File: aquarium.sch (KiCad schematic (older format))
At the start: 39 parts, among them U1 MOC3063, U2 MOC3063

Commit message: ATmega48PA changet to ATmega8A
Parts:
- DD4: value ATMEGA48PA -> ATMEGA8A; symbol ATMEGA48PA_EXT -> ATMEGA8_EXT
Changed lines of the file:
@@
 $EndDescr
 $Comp
-L ATMEGA48PA_EXT DD4
+L ATMEGA8_EXT DD4
 U 1 1 5677FF09
 P 10150 2900
 F 0 "DD4" H 10150 5101 138 0000 C CNN
-F 1 "ATMEGA48PA" H 10150 4886 138 0000 C CNN
+F 1 "ATMEGA8A" H 10150 4886 138 0000 C CNN
 F 2 "Микросхемы:TQFP32-30" H 10150 4831 60  0001 C CNN
 F 3 "" H 10150 3150 60  0001 C CNN

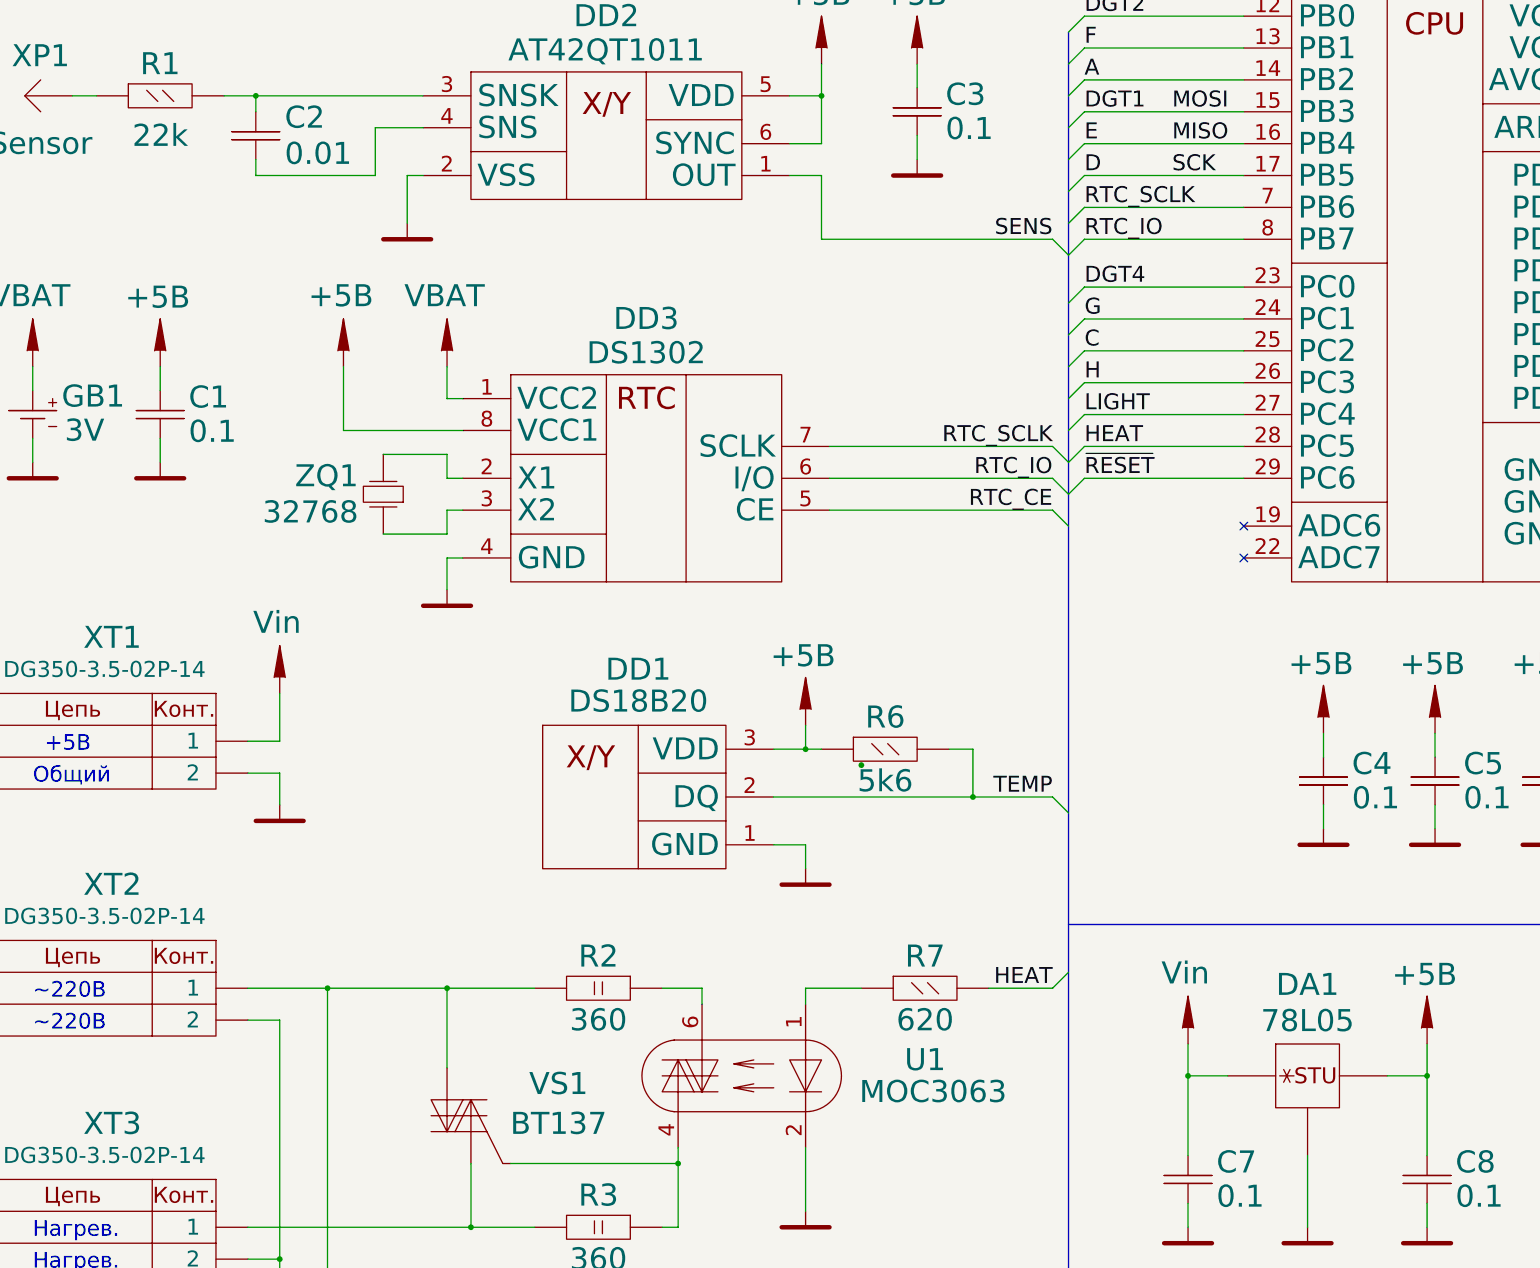
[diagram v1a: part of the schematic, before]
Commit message: Corrected sensitivity of the sensor and added noise protection on Reset pin.
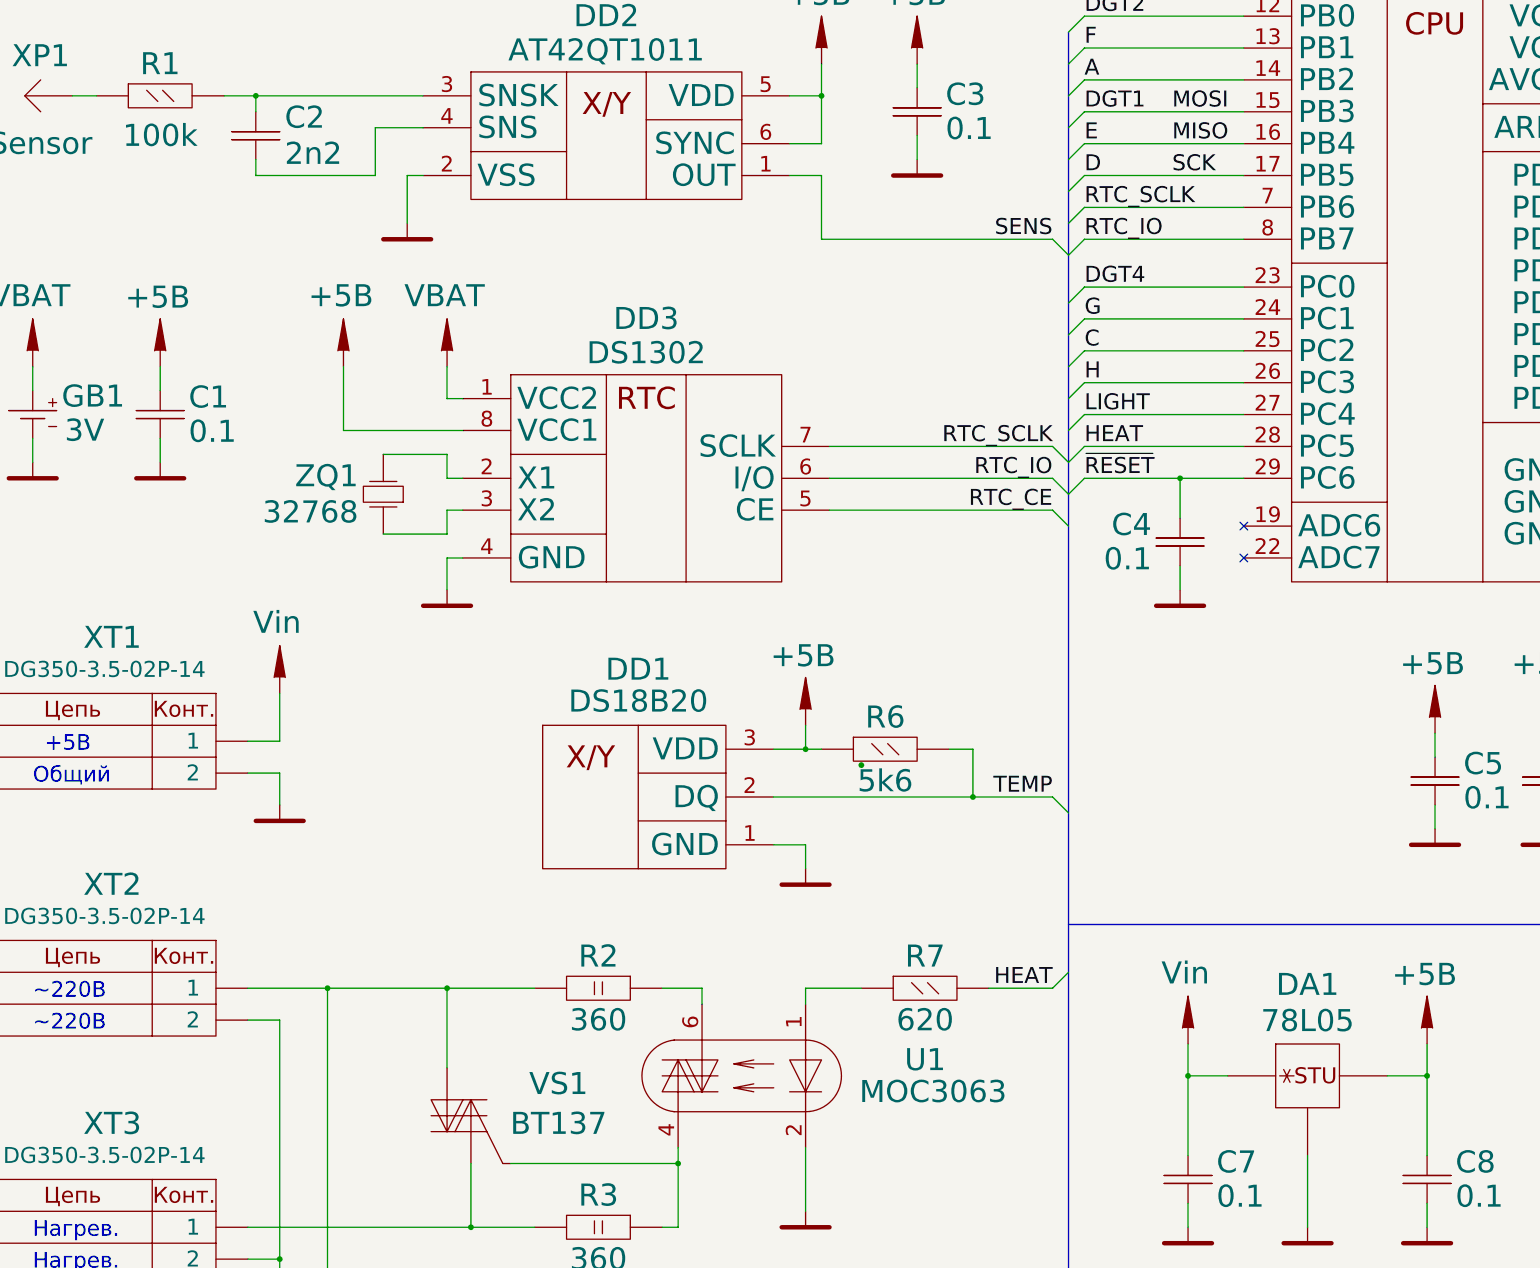
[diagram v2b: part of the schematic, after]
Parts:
- C2: value 0.01 -> 2n2
- R1: value 22k -> 100k
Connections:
- net +5B: no longer C4.1
- net ~RESET: now also C4.1
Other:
- moved on the sheet: C4
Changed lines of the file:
@@
 L C C4
 U 1 1 5679197E
-P 9450 6000
-F 0 "C4" H 9628 6108 138 0000 L CNN
-F 1 "0.1" H 9628 5893 138 0000 L CNN
-F 2 "Конденсаторы:SMD_0805" H 9450 6025 60  0001 C CNN
-F 3 "" H 9450 6025 60  0000 C CNN
-	1    9450 6000
-	1    0    0    -1
+P 8550 4500
+F 0 "C4" H 8728 4608 138 0000 L CNN
+F 1 "0.1" H 8728 4393 138 0000 L CNN
+F 2 "Конденсаторы:SMD_0805" H 8550 4525 60  0001 C CNN
+F 3 "" H 8550 4525 60  0000 C CNN
+	1    8550 4500
+	-1   0    0    -1
 $EndComp
 $Comp
@@
 L GND #PWR01
 U 1 1 56791BC2
-P 9450 6300
-F 0 "#PWR01" H 9850 6300 138 0001 C CNN
-F 1 "GND" H 9100 6300 138 0001 C CNN
-F 2 "" H 9450 6300 60  0000 C CNN
-F 3 "" H 9450 6300 60  0000 C CNN
-	1    9450 6300
-	1    0    0    -1
+P 8550 4800
+F 0 "#PWR01" H 8950 4800 138 0001 C CNN
+F 1 "GND" H 8200 4800 138 0001 C CNN
+F 2 "" H 8550 4800 60  0000 C CNN
+F 3 "" H 8550 4800 60  0000 C CNN
+	1    8550 4800
+	-1   0    0    -1
 $EndComp
 $Comp
@@
 $Comp
 L +5B #PWR04
-U 1 1 56791C22
-P 9450 5700
-F 0 "#PWR04" H 9950 5800 138 0001 C CNN
-F 1 "+5B" H 9434 6135 138 0000 C CNN
-F 2 "" H 9450 5900 60  0000 C CNN
-F 3 "" H 9450 5900 60  0000 C CNN
-	1    9450 5700
-	1    0    0    -1
-$EndComp
-$Comp
-L +5B #PWR05
 U 1 1 56791C40
 P 10150 5700
-F 0 "#PWR05" H 10650 5800 138 0001 C CNN
+F 0 "#PWR04" H 10650 5800 138 0001 C CNN
 F 1 "+5B" H 10134 6135 138 0000 C CNN
 F 2 "" H 10150 5900 60  0000 C CNN
@@
 $EndComp
 $Comp
-L +5B #PWR06
+L +5B #PWR05
 U 1 1 56791C61
 P 10850 5700
-F 0 "#PWR06" H 11350 5800 138 0001 C CNN
+F 0 "#PWR05" H 11350 5800 138 0001 C CNN
 F 1 "+5B" H 10834 6135 138 0000 C CNN
 F 2 "" H 10850 5900 60  0000 C CNN
@@
 $EndComp
 Wire Wire Line
-	9450 5700 9450 5850
-Wire Wire Line
-	9450 6150 9450 6300
+	8550 4100 8550 4350
+Wire Wire Line
+	8550 4650 8550 4800
 Wire Wire Line
 	10150 5700 10150 5850
@@
 	10850 6150 10850 6300
 $Comp
-L +5B #PWR07
+L +5B #PWR06
 U 1 1 56791F4C
 P 11550 1000
-F 0 "#PWR07" H 12050 1100 138 0001 C CNN
+F 0 "#PWR06" H 12050 1100 138 0001 C CNN
 F 1 "+5B" H 11534 1435 138 0000 C CNN
 F 2 "" H 11550 1200 60  0000 C CNN
@@
 Connection ~ 11550 1200
 $Comp
-L GND #PWR08
+L GND #PWR07
 U 1 1 567920EA
 P 11550 4800
-F 0 "#PWR08" H 11950 4800 138 0001 C CNN
+F 0 "#PWR07" H 11950 4800 138 0001 C CNN
 F 1 "GND" H 11200 4800 138 0001 C CNN
 F 2 "" H 11550 4800 60  0000 C CNN
@@
 $EndComp
 $Comp
-L GND #PWR09
+L GND #PWR08
 U 1 1 56795326
 P 6900 2100
-F 0 "#PWR09" H 7300 2100 138 0001 C CNN
+F 0 "#PWR08" H 7300 2100 138 0001 C CNN
 F 1 "GND" H 6550 2100 138 0001 C CNN
 F 2 "" H 6900 2100 60  0000 C CNN
@@
 $EndComp
 $Comp
-L +5B #PWR010
+L +5B #PWR09
 U 1 1 5679532C
 P 6900 1500
-F 0 "#PWR010" H 7400 1600 138 0001 C CNN
+F 0 "#PWR09" H 7400 1600 138 0001 C CNN
 F 1 "+5B" H 6884 1935 138 0000 C CNN
 F 2 "" H 6900 1700 60  0000 C CNN
@@
 $EndComp
 $Comp
-L GND #PWR011
+L GND #PWR010
 U 1 1 567953A0
 P 2150 4000
-F 0 "#PWR011" H 2550 4000 138 0001 C CNN
+F 0 "#PWR010" H 2550 4000 138 0001 C CNN
 F 1 "GND" H 1800 4000 138 0001 C CNN
 F 2 "" H 2150 4000 60  0000 C CNN
@@
 $EndComp
 $Comp
-L +5B #PWR012
+L +5B #PWR011
 U 1 1 567953A6
 P 2150 3400
-F 0 "#PWR012" H 2650 3500 138 0001 C CNN
+F 0 "#PWR011" H 2650 3500 138 0001 C CNN
 F 1 "+5B" H 2134 3835 138 0000 C CNN
 F 2 "" H 2150 3600 60  0000 C CNN
@@
 	3950 3950 3550 3950
 $Comp
-L GND #PWR013
+L GND #PWR012
 U 1 1 567978D5
 P 1350 4000
-F 0 "#PWR013" H 1750 4000 138 0001 C CNN
+F 0 "#PWR012" H 1750 4000 138 0001 C CNN
 F 1 "GND" H 1000 4000 138 0001 C CNN
 F 2 "" H 1350 4000 60  0000 C CNN
@@
 $EndComp
 $Comp
-L VBAT #PWR014
+L VBAT #PWR013
 U 1 1 56797B2B
 P 1350 3400
-F 0 "#PWR014" H 1850 3500 138 0001 C CNN
+F 0 "#PWR013" H 1850 3500 138 0001 C CNN
 F 1 "VBAT" H 1334 3844 138 0000 C CNN
 F 2 "" H 1350 3600 60  0000 C CNN
@@
 	1350 3850 1350 4000
 $Comp
-L +5B #PWR015
+L +5B #PWR014
 U 1 1 56797DB1
 P 3300 3400
-F 0 "#PWR015" H 3800 3500 138 0001 C CNN
+F 0 "#PWR014" H 3800 3500 138 0001 C CNN
 F 1 "+5B" H 3284 3844 138 0000 C CNN
 F 2 "" H 3300 3600 60  0000 C CNN
@@
 $EndComp
 $Comp
-L VBAT #PWR016
+L VBAT #PWR015
 U 1 1 56797DDB
 P 3950 3400
-F 0 "#PWR016" H 4450 3500 138 0001 C CNN
+F 0 "#PWR015" H 4450 3500 138 0001 C CNN
 F 1 "VBAT" H 3934 3844 138 0000 C CNN
 F 2 "" H 3950 3600 60  0000 C CNN
@@
 P 2750 1950
 F 0 "C2" H 2931 2064 138 0000 L CNN
-F 1 "0.01" H 2931 1837 138 0000 L CNN
+F 1 "2n2" H 2931 1837 138 0000 L CNN
 F 2 "Конденсаторы:SMD_0805" H 2750 1975 60  0001 C CNN
 F 3 "" H 2750 1975 60  0000 C CNN
@@
 $EndComp
 $Comp
-L GND #PWR017
+L GND #PWR016
 U 1 1 5679847B
 P 3950 4800
-F 0 "#PWR017" H 4350 4800 138 0001 C CNN
+F 0 "#PWR016" H 4350 4800 138 0001 C CNN
 F 1 "GND" H 3600 4800 138 0001 C CNN
 F 2 "" H 3950 4800 60  0000 C CNN
@@
 	2750 2200 2750 2100
 $Comp
-L GND #PWR018
+L GND #PWR017
 U 1 1 56798CBF
 P 3700 2500
-F 0 "#PWR018" H 4100 2500 138 0001 C CNN
+F 0 "#PWR017" H 4100 2500 138 0001 C CNN
 F 1 "GND" H 3350 2500 138 0001 C CNN
 F 2 "" H 3700 2500 60  0000 C CNN
@@
 	3700 2200 3700 2500
 $Comp
-L +5B #PWR019
+L +5B #PWR018
 U 1 1 56798EC0
 P 6300 1500
-F 0 "#PWR019" H 6800 1600 138 0001 C CNN
+F 0 "#PWR018" H 6800 1600 138 0001 C CNN
 F 1 "+5B" H 6284 1935 138 0000 C CNN
 F 2 "" H 6300 1700 60  0000 C CNN
@@
 P 2150 1700
 F 0 "R1" H 2150 1900 138 0000 C CNN
-F 1 "22k" H 2150 1450 138 0000 C CNN
+F 1 "100k" H 2150 1450 138 0000 C CNN
 F 2 "Резисторы:R_0805" H 2150 1700 60  0001 C CNN
 F 3 "" H 2150 1700 60  0000 C CNN
@@
 $EndComp
 $Comp
-L +5B #PWR020
+L +5B #PWR019
 U 1 1 567A523E
 P 6200 5650
-F 0 "#PWR020" H 6700 5750 138 0001 C CNN
+F 0 "#PWR019" H 6700 5750 138 0001 C CNN
 F 1 "+5B" H 6184 6085 138 0000 C CNN
 F 2 "" H 6200 5850 60  0000 C CNN
@@
 	6000 5800 6300 5800
 $Comp
-L GND #PWR021
+L GND #PWR020
 U 1 1 567A531F
 P 6200 6550
-F 0 "#PWR021" H 6600 6550 138 0001 C CNN
+F 0 "#PWR020" H 6600 6550 138 0001 C CNN
 F 1 "GND" H 5850 6550 138 0001 C CNN
 F 2 "" H 6200 6550 60  0000 C CNN
@@
 	2700 11000 4500 11000
 $Comp
-L GND #PWR022
+L GND #PWR021
 U 1 1 567B4547
 P 6200 8700
-F 0 "#PWR022" H 6600 8700 138 0001 C CNN
+F 0 "#PWR021" H 6600 8700 138 0001 C CNN
 F 1 "GND" H 5850 8700 138 0001 C CNN
 F 2 "" H 6200 8700 60  0000 C CNN
@@
 $EndComp
 $Comp
-L GND #PWR023
+L GND #PWR022
 U 1 1 567B47F5
 P 6200 10900
-F 0 "#PWR023" H 6600 10900 138 0001 C CNN
+F 0 "#PWR022" H 6600 10900 138 0001 C CNN
 F 1 "GND" H 5850 10900 138 0001 C CNN
 F 2 "" H 6200 10900 60  0000 C CNN
@@
 Общий
 $Comp
-L GND #PWR024
+L GND #PWR023
 U 1 1 567D101C
 P 2900 6150
-F 0 "#PWR024" H 3300 6150 138 0001 C CNN
+F 0 "#PWR023" H 3300 6150 138 0001 C CNN
 F 1 "GND" H 2550 6150 138 0001 C CNN
 F 2 "" H 2900 6150 60  0000 C CNN
@@
 	2900 5950 2900 6150
 $Comp
-L +5B #PWR025
+L +5B #PWR024
 U 1 1 567D1252
 P 10100 7650
-F 0 "#PWR025" H 10600 7750 138 0001 C CNN
+F 0 "#PWR024" H 10600 7750 138 0001 C CNN
 F 1 "+5B" H 10084 8085 138 0000 C CNN
 F 2 "" H 10100 7850 60  0000 C CNN
@@
 $EndComp
 $Comp
-L Vin #PWR026
+L Vin #PWR025
 U 1 1 567FEE18
 P 2900 5450
-F 0 "#PWR026" H 3400 5550 138 0001 C CNN
+F 0 "#PWR025" H 3400 5550 138 0001 C CNN
 F 1 "Vin" H 2884 5894 138 0000 C CNN
 F 2 "" H 2900 5650 60  0000 C CNN
@@
 	2900 5750 2700 5750
 $Comp
-L Vin #PWR027
+L Vin #PWR026
 U 1 1 567FF0F3
 P 8600 7650
-F 0 "#PWR027" H 9100 7750 138 0001 C CNN
+F 0 "#PWR026" H 9100 7750 138 0001 C CNN
 F 1 "Vin" H 8584 8094 138 0000 C CNN
 F 2 "" H 8600 7850 60  0000 C CNN
@@
 $EndComp
 $Comp
-L GND #PWR028
+L GND #PWR027
 U 1 1 567FF2BB
 P 8600 8800
-F 0 "#PWR028" H 9000 8800 138 0001 C CNN
+F 0 "#PWR027" H 9000 8800 138 0001 C CNN
 F 1 "GND" H 8250 8800 138 0001 C CNN
 F 2 "" H 8600 8800 60  0000 C CNN
@@
 $EndComp
 $Comp
-L GND #PWR029
+L GND #PWR028
 U 1 1 567FF36E
 P 10100 8800
-F 0 "#PWR029" H 10500 8800 138 0001 C CNN
+F 0 "#PWR028" H 10500 8800 138 0001 C CNN
 F 1 "GND" H 9750 8800 138 0001 C CNN
 F 2 "" H 10100 8800 60  0000 C CNN
@@
 Connection ~ 8600 7850
 Wire Wire Line
-	10100 8350 10100 7650
+	10100 7650 10100 8350
 Wire Wire Line
 	9850 7850 10100 7850
 Connection ~ 10100 7850
 $Comp
-L GND #PWR030
+L GND #PWR029
 U 1 1 567FF75B
 P 9350 8800
-F 0 "#PWR030" H 9750 8800 138 0001 C CNN
+F 0 "#PWR029" H 9750 8800 138 0001 C CNN
 F 1 "GND" H 9000 8800 138 0001 C CNN
 F 2 "" H 9350 8800 60  0000 C CNN
@@
 	9350 8350 9350 8800
 Connection ~ 6550 5900
+Connection ~ 8550 4100
 $EndSCHEMATC
